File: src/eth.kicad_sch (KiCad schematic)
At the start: 43 parts, among them J9 ARJM11C7-114-BA-EW2, U27 USBLC6-4SC6, U28 LAN8742A, Y2 25MHz

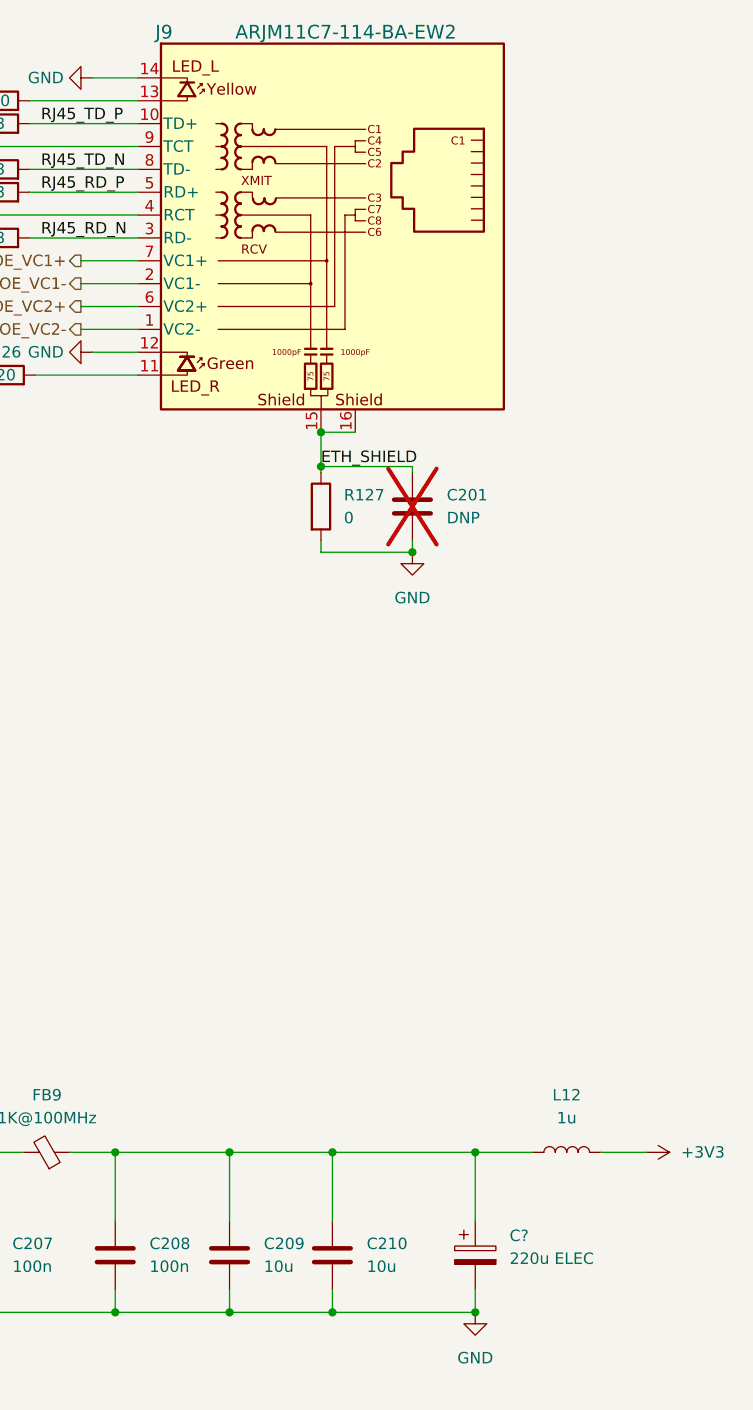
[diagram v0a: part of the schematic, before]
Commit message: Fix issiues from lis, see bug/issiue list in DOC directory
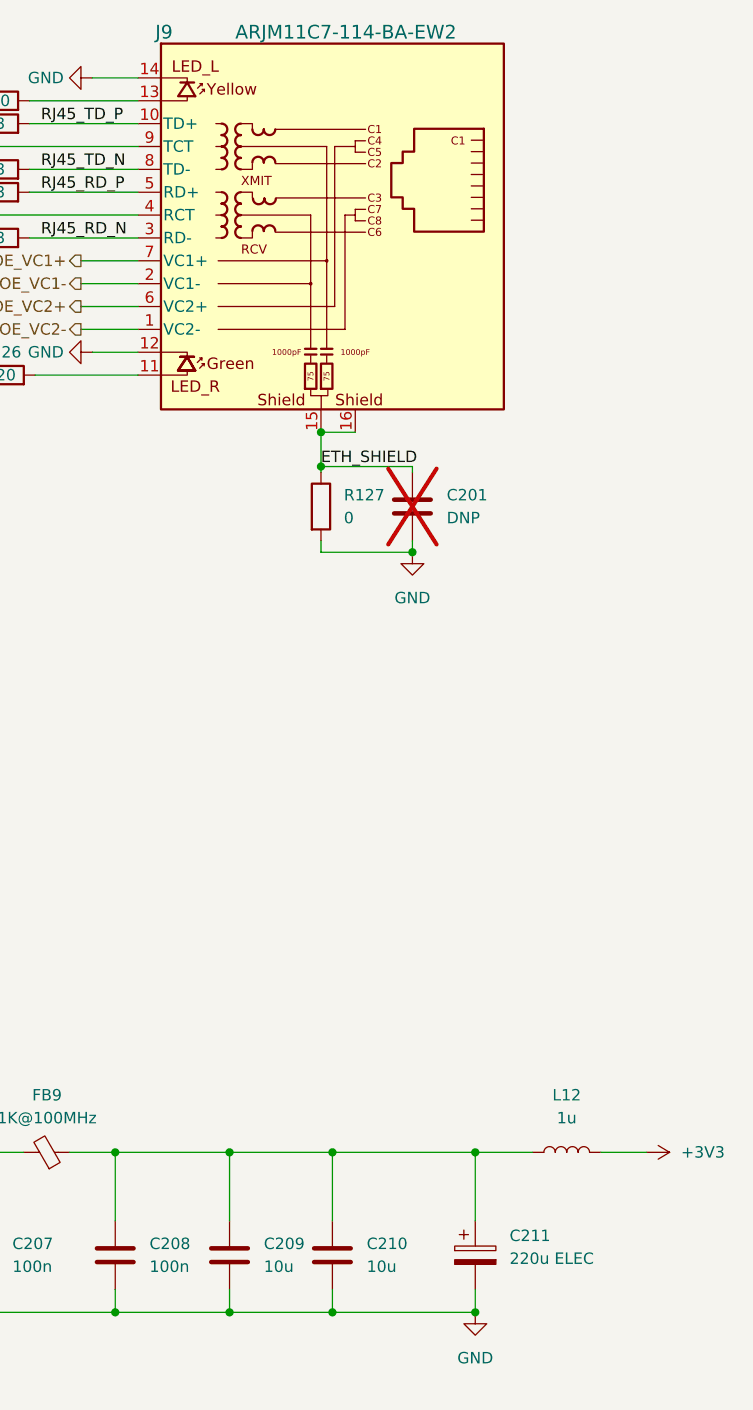
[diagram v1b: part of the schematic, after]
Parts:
- gave numbers to parts that had none: 1
